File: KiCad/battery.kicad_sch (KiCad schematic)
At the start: 1 part

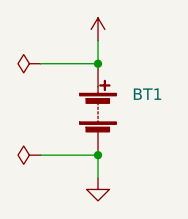
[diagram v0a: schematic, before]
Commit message: feat(pcb): add input capacitors
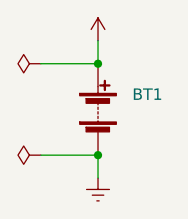
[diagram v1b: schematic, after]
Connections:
- net GND renamed GNDREF
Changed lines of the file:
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@@
 (kicad_sch (version 20211123) (generator eeschema)
   (paper "A4")
+  (junction (at 139.7 88.9) (diameter 0) (color 0 0 0 0)
+  )
   (junction (at 139.7 99.06) (diameter 0) (color 0 0 0 0)
-  )
-  (junction (at 139.7 88.9) (diameter 0) (color 0 0 0 0)
   )
   (wire (pts (xy 139.7 86.36) (xy 139.7 88.9))
@@
   (wire (pts (xy 133.35 99.06) (xy 139.7 99.06))
     (stroke (width 0) (type default) (color 0 0 0 0))
-  )
-  (symbol (lib_id "power:GND") (at 139.7 101.6 0) (unit 1)
-    (in_bom yes) (on_board yes) (fields_autoplaced)
-    (property "Reference" "#PWR0101" (id 0) (at 139.7 107.95 0)
-      (effects (font (size 1.27 1.27)) hide)
-    )
-    (property "Value" "" (id 1) (at 139.7 106.68 0))
-    (property "Footprint" "" (id 2) (at 139.7 101.6 0)
-      (effects (font (size 1.27 1.27)) hide)
-    )
-    (property "Datasheet" "" (id 3) (at 139.7 101.6 0)
-      (effects (font (size 1.27 1.27)) hide)
-    )
-    (pin "1")
   )
   (symbol (lib_id "power:PWR_FLAG") (at 133.35 99.06 90) (unit 1)
@@
       (effects (font (size 1.27 1.27)) hide)
     )
+    (pin "1")
+  )
+  (symbol (lib_id "power:GNDREF") (at 139.7 101.6 0) (unit 1)
+    (in_bom yes) (on_board yes) (fields_autoplaced)
+    (property "Reference" "#PWR0103" (id 0) (at 139.7 107.95 0)
+      (effects (font (size 1.27 1.27)) hide)
+    )
+    (property "Value" "" (id 1) (at 139.7 106.68 0))
+    (property "Footprint" "" (id 2) (at 139.7 101.6 0)
+      (effects (font (size 1.27 1.27)) hide)
+    )
+    (property "Datasheet" "" (id 3) (at 139.7 101.6 0)
+      (effects (font (size 1.27 1.27)) hide)
+    )

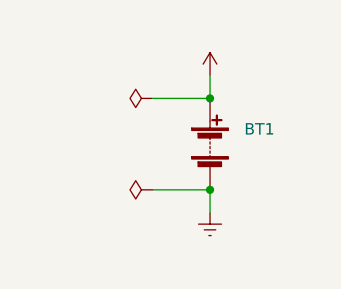
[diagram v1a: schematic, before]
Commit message: feat(pcb): add footprints
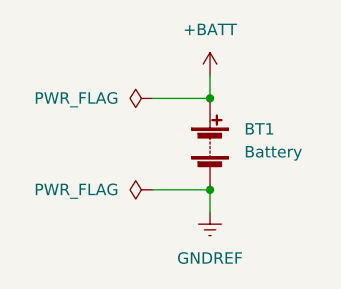
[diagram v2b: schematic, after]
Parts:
- BT1: value (none) -> Battery; now left out of the parts list
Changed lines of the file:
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@@
       (effects (font (size 1.27 1.27)) hide)
     )
-    (property "Value" "" (id 1) (at 129.54 99.0599 90)
+    (property "Value" "PWR_FLAG" (id 1) (at 129.54 99.0599 90)
       (effects (font (size 1.27 1.27)) (justify left))
     )
@@
       (effects (font (size 1.27 1.27)) hide)
     )
-    (property "Value" "" (id 1) (at 129.54 88.8999 90)
+    (property "Value" "PWR_FLAG" (id 1) (at 129.54 88.8999 90)
       (effects (font (size 1.27 1.27)) (justify left))
     )
@@
       (effects (font (size 1.27 1.27)) hide)
     )
-    (property "Value" "" (id 1) (at 139.7 81.28 0))
+    (property "Value" "+BATT" (id 1) (at 139.7 81.28 0))
     (property "Footprint" "" (id 2) (at 139.7 86.36 0)
       (effects (font (size 1.27 1.27)) hide)
@@
       (effects (font (size 1.27 1.27)) hide)
     )
-    (property "Value" "" (id 1) (at 139.7 106.68 0))
+    (property "Value" "GNDREF" (id 1) (at 139.7 106.68 0))
     (property "Footprint" "" (id 2) (at 139.7 101.6 0)
       (effects (font (size 1.27 1.27)) hide)
@@
   )
   (symbol (lib_id "Device:Battery") (at 139.7 93.98 0) (unit 1)
-    (in_bom yes) (on_board yes) (fields_autoplaced)
+    (in_bom no) (on_board no) (fields_autoplaced)
     (property "Reference" "BT1" (id 0) (at 143.51 92.3289 0)
       (effects (font (size 1.27 1.27)) (justify left))
     )
-    (property "Value" "" (id 1) (at 143.51 94.8689 0)
+    (property "Value" "Battery" (id 1) (at 143.51 94.8689 0)
       (effects (font (size 1.27 1.27)) (justify left))
     )

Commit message: feat(pcb): add mounting holes
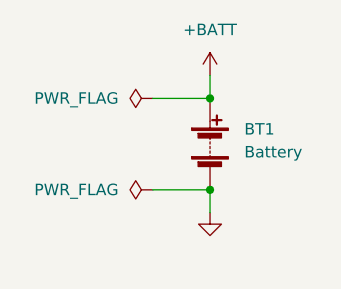
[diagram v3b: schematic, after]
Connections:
- net GNDREF renamed GND
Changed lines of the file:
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@@
     (pin "1")
   )
-  (symbol (lib_id "power:GNDREF") (at 139.7 101.6 0) (unit 1)
+  (symbol (lib_id "power:GND") (at 139.7 101.6 0) (unit 1)
     (in_bom yes) (on_board yes) (fields_autoplaced)
     (property "Reference" "#PWR0103" (id 0) (at 139.7 107.95 0)
       (effects (font (size 1.27 1.27)) hide)
     )
-    (property "Value" "GNDREF" (id 1) (at 139.7 106.68 0))
+    (property "Value" "" (id 1) (at 139.7 106.68 0))
     (property "Footprint" "" (id 2) (at 139.7 101.6 0)
       (effects (font (size 1.27 1.27)) hide)

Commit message: feat(pcb): add schematic for connectors
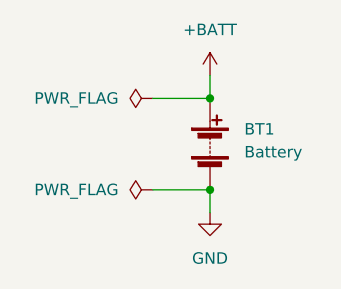
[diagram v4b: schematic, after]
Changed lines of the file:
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@@
       (effects (font (size 1.27 1.27)) hide)
     )
-    (property "Value" "" (id 1) (at 139.7 106.68 0))
+    (property "Value" "GND" (id 1) (at 139.7 106.68 0))
     (property "Footprint" "" (id 2) (at 139.7 101.6 0)
       (effects (font (size 1.27 1.27)) hide)
